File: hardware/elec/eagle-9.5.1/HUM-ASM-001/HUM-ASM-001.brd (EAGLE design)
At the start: 99.1 x 99.1 mm, 61 parts, among them J1 B2B-XH-AM(LF)(SN), J2 75869-131LF, J22 75869-131LF, J23 75869-131LF, K1 7-1393239-7, K2 7-1393239-7, Q1 IRLB8721PBF, Q2 IRLB8721PBF, U1 MCP23017-E/SP

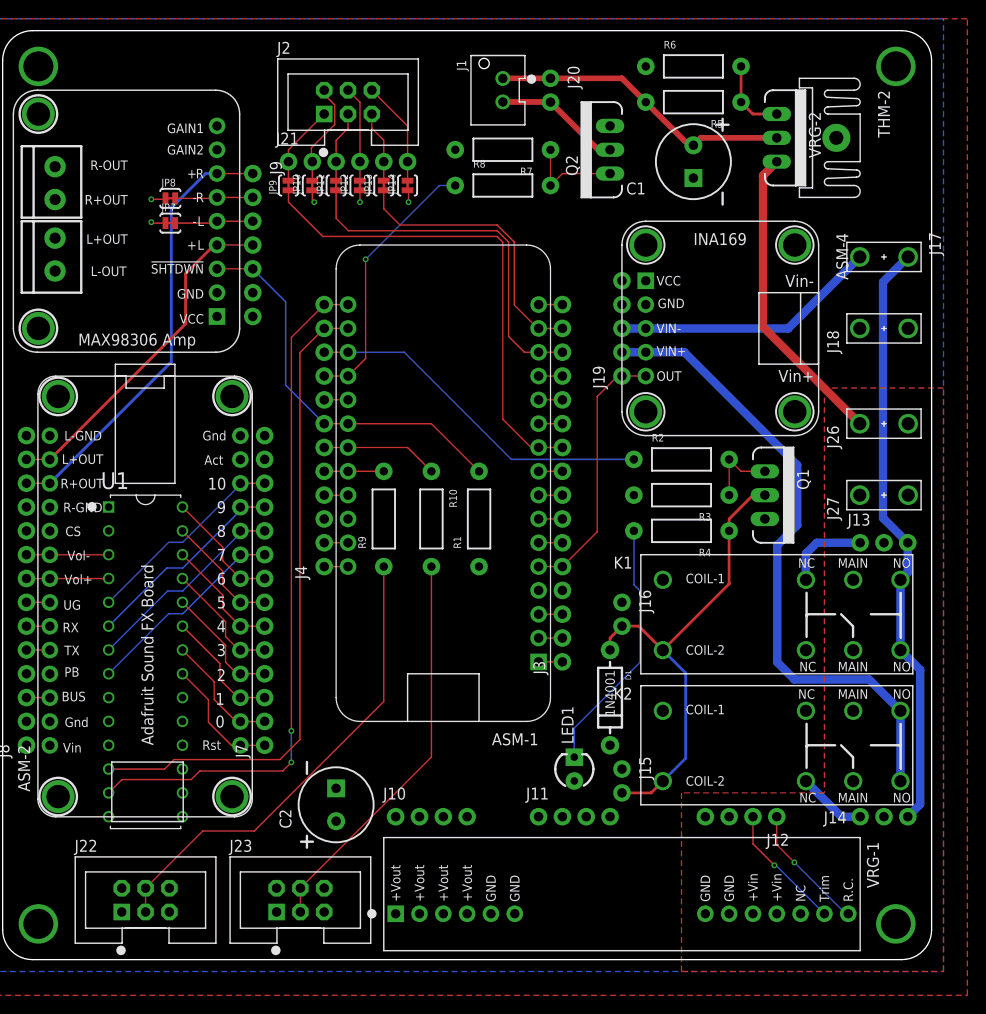
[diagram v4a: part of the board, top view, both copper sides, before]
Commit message: * Fixed crash / recovery inconsistency * Pre silk screen clean up
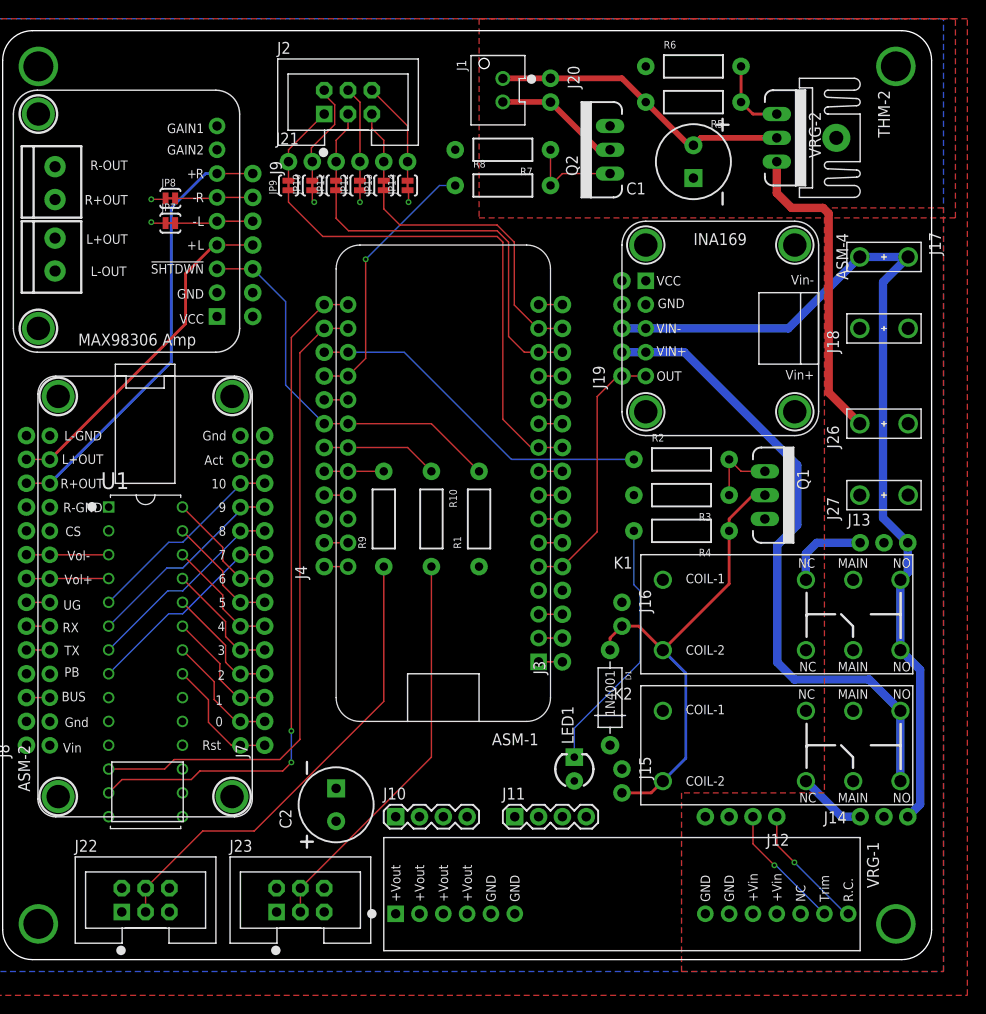
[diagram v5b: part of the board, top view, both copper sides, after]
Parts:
- J10, J11: device MG-Eagle_v1:1X04_NO_SILK_ALL_ROUND -> MG-Eagle_v1:1X04
- moved J11 2.54 mm to (54.6, 15.2)
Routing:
- net MIST-VIN: track 92.2 -> 97.3 mm
- net N$26: track 0.00 -> 2.59 mm
- net 48V: track 32.8 -> 33.6 mm
- added copper zone on layer 1, net 24V-CUTOUT
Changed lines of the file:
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@@
 <setting verticaltext="up"/>
 </settings>
-<grid distance="0.012" unitdist="inch" unit="inch" style="dots" multiple="1" display="yes" altdistance="0.006" altunitdist="inch" altunit="inch"/>
+<grid distance="0.05" unitdist="inch" unit="inch" style="dots" multiple="1" display="yes" altdistance="0.005" altunitdist="inch" altunit="inch"/>
 <layers>
 <layer number="1" name="Top" color="12" fill="1" visible="yes" active="yes"/>
@@
 <layer number="25" name="tNames" color="16" fill="1" visible="yes" active="yes"/>
 <layer number="26" name="bNames" color="7" fill="1" visible="yes" active="yes"/>
-<layer number="27" name="tValues" color="16" fill="1" visible="yes" active="yes"/>
-<layer number="28" name="bValues" color="7" fill="1" visible="yes" active="yes"/>
-<layer number="29" name="tStop" color="7" fill="3" visible="no" active="yes"/>
-<layer number="30" name="bStop" color="7" fill="6" visible="no" active="yes"/>
+<layer number="27" name="tValues" color="16" fill="1" visible="no" active="yes"/>
+<layer number="28" name="bValues" color="7" fill="1" visible="no" active="yes"/>
+<layer number="29" name="tStop" color="7" fill="3" visible="yes" active="yes"/>
+<layer number="30" name="bStop" color="7" fill="6" visible="yes" active="yes"/>
 <layer number="31" name="tCream" color="7" fill="4" visible="no" active="yes"/>
 <layer number="32" name="bCream" color="7" fill="5" visible="no" active="yes"/>
@@
 <layer number="45" name="Holes" color="7" fill="1" visible="yes" active="yes"/>
 <layer number="46" name="Milling" color="20" fill="1" visible="yes" active="yes"/>
-<layer number="47" name="Measures" color="5" fill="1" visible="no" active="yes"/>
+<layer number="47" name="Measures" color="5" fill="1" visible="yes" active="yes"/>
 <layer number="48" name="Document" color="6" fill="1" visible="yes" active="yes"/>
 <layer number="49" name="Reference" color="5" fill="1" visible="yes" active="yes"/>
@@
 <attribute name="VALUE" x="48.036" y="95.926" size="0.762" layer="27" ratio="11" rot="R270" align="top-left"/>
 </element>
-<element name="J10" library="MG-Eagle_v1" package="1X04_NO_SILK_ALL_ROUND" value="" x="41.91" y="15.24" smashed="yes">
+<element name="J10" library="MG-Eagle_v1" package="1X04" value="" x="41.91" y="15.24" smashed="yes">
 <attribute name="NAME" x="40.5638" y="17.0688" size="1.27" layer="25" ratio="10"/>
 <attribute name="PROD_ID" value="CONN-09696" x="146.05" y="-137.16" size="1.778" layer="27" display="off"/>
 <attribute name="VALUE" x="40.64" y="12.065" size="1.27" layer="27"/>
 </element>
-<element name="J11" library="MG-Eagle_v1" package="1X04_NO_SILK_ALL_ROUND" value="" x="57.15" y="15.24" smashed="yes">
-<attribute name="NAME" x="55.8038" y="17.0688" size="1.27" layer="25" ratio="10"/>
-<attribute name="PROD_ID" value="CONN-09696" x="172.72" y="-137.16" size="1.778" layer="27" display="off"/>
-<attribute name="VALUE" x="55.88" y="12.065" size="1.27" layer="27"/>
+<element name="J11" library="MG-Eagle_v1" package="1X04" value="" x="54.61" y="15.24" smashed="yes">
+<attribute name="NAME" x="53.2638" y="17.0688" size="1.27" layer="25" ratio="10"/>
+<attribute name="PROD_ID" value="CONN-09696" x="170.18" y="-137.16" size="1.778" layer="27" display="off"/>
+<attribute name="VALUE" x="53.34" y="12.065" size="1.27" layer="27"/>
 </element>
 <element name="J12" library="MG-Eagle_v1" package="1X04_NO_SILK_ALL_ROUND" value="" x="82.55" y="15.24" smashed="yes" rot="R180">
@@
 <wire x1="17.3736" y1="78.5368" x2="15.9512" y2="78.5368" width="0.1524" layer="1"/>
 <wire x1="15.9512" y1="78.5368" x2="15.8496" y2="78.6384" width="0.1524" layer="1"/>
+<wire x1="91.4019" y1="49.53" x2="96.5581" y2="49.53" width="0" layer="19" extent="1-1"/>
 </signal>
 <signal name="5V">
@@
 <contactref element="J26" pad="2"/>
 <polygon width="0.3048" layer="1" isolate="0.8128">
-<vertex x="100.33" y="60.96"/>
-<vertex x="87.63" y="60.96"/>
+<vertex x="100.33" y="80.1624"/>
+<vertex x="87.63" y="80.1624"/>
 <vertex x="87.63" y="17.78"/>
 <vertex x="72.39" y="17.78"/>
@@
 <vertex x="100.33" y="-1.27"/>
 </polygon>
-<wire x1="91.4019" y1="57.15" x2="81.0768" y2="67.4751" width="0.889" layer="1"/>
-<wire x1="81.0768" y1="83.6168" x2="82.55" y2="85.09" width="0.889" layer="1"/>
-<wire x1="81.0768" y1="67.4751" x2="81.0768" y2="83.6168" width="0.889" layer="1"/>
+<wire x1="91.4019" y1="57.15" x2="88.0872" y2="60.4647" width="0.889" layer="1"/>
+<wire x1="87.4776" y1="80.1624" x2="84.1248" y2="80.1624" width="0.889" layer="1"/>
+<wire x1="84.1248" y1="80.1624" x2="82.55" y2="81.7372" width="0.889" layer="1"/>
+<wire x1="82.55" y1="81.7372" x2="82.55" y2="85.09" width="0.889" layer="1"/>
+<wire x1="88.0872" y1="60.4647" x2="88.0872" y2="79.5528" width="0.889" layer="1"/>
+<wire x1="88.0872" y1="79.5528" x2="87.4776" y2="80.1624" width="0.889" layer="1"/>
 </signal>
 <signal name="N$27">
@@
 <wire x1="97.8408" y1="30.8992" x2="95.74" y2="33" width="0.889" layer="16"/>
 <wire x1="97.8408" y1="16.5608" x2="97.8408" y2="30.8992" width="0.889" layer="16"/>
-<wire x1="96.5581" y1="74.93" x2="91.4019" y2="74.93" width="0" layer="19" extent="1-1"/>
+<wire x1="91.4019" y1="74.93" x2="96.5581" y2="74.93" width="0.889" layer="16"/>
 </signal>
 <signal name="N$16">
@@
 <contactref element="ASM-2" pad="13"/>
 <contactref element="J7" pad="13"/>
-<wire x1="25.351" y1="53.327" x2="27.94" y2="53.34" width="0" layer="19" extent="1-1"/>
+<wire x1="25.351" y1="53.327" x2="25.364" y2="53.34" width="0.1524" layer="1"/>
+<wire x1="25.364" y1="53.34" x2="27.94" y2="53.34" width="0.1524" layer="1"/>
 </signal>
 <signal name="USB/VBUS">
@@
 <wire x1="22.7584" y1="81.1784" x2="22.86" y2="81.28" width="0.1524" layer="1"/>
 </signal>
+<signal name="24V-CUTOUT">
+<polygon width="0.3048" layer="1" pour="cutout" isolate="0.3048" rank="2">
+<vertex x="50.8" y="100.33"/>
+<vertex x="50.8" y="79.0956"/>
+<vertex x="101.6" y="79.0956"/>
+<vertex x="101.6" y="100.33"/>
+</polygon>
+</signal>
 </signals>

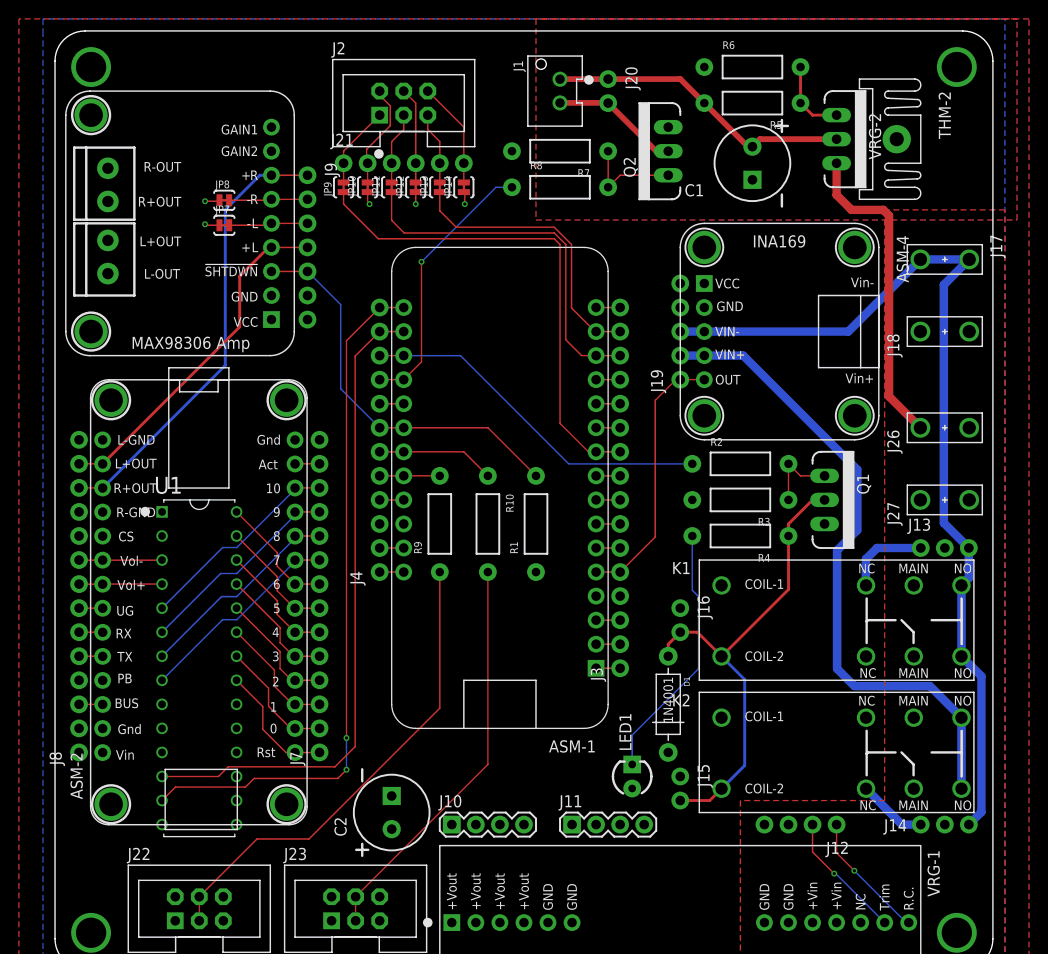
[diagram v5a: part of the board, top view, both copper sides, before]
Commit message: * Normalized Text for Names and Values
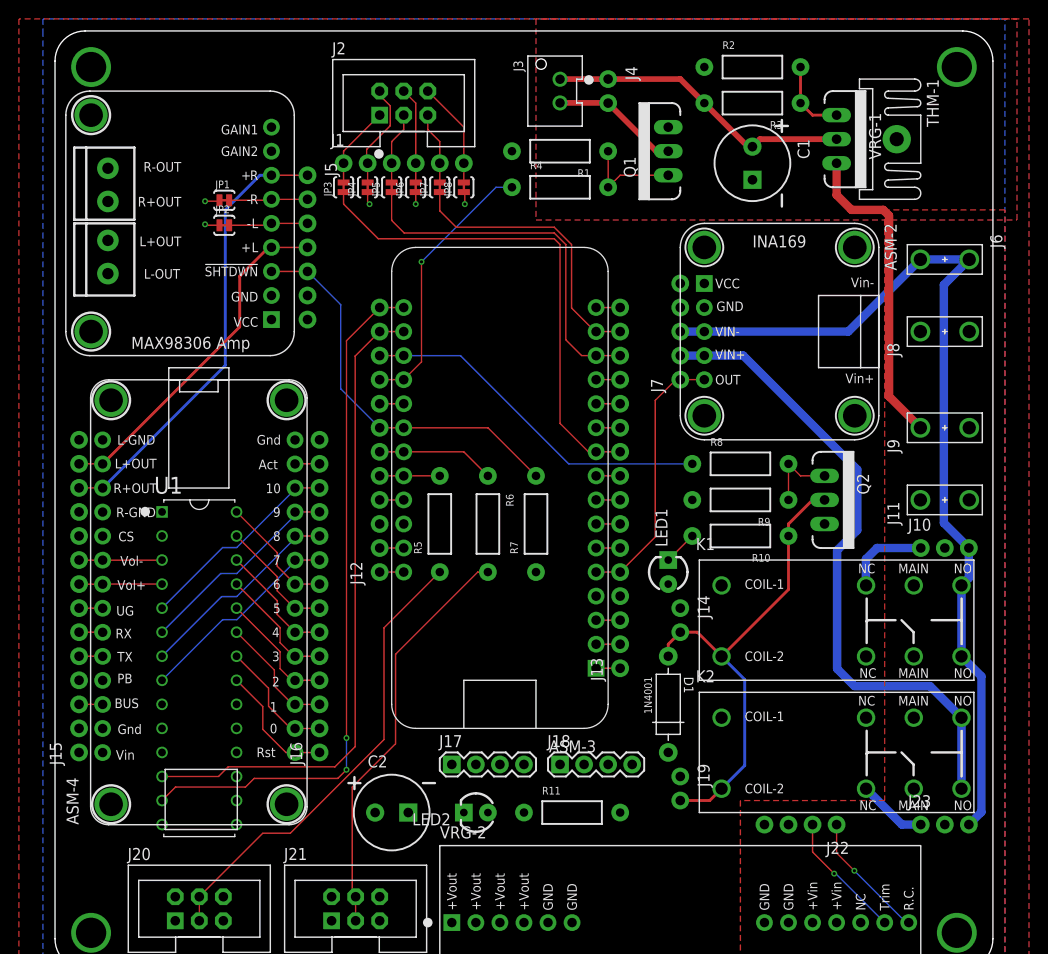
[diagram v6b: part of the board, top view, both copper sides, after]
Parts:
- removed J26, J27: (no value), MG-Eagle_v1:TE_1217861-1
- removed JP13, JP14: CON_JUMPER_PAD-2-NC_BY_TRACE, MG-Eagle_v1:PAD-JUMPER-2-NC_BY_TRACE_YES_SILK
- added J5: (no value), MG-Eagle_v1:1X07_NO_SILK
- added J6: (no value), MG-Eagle_v1:TE_1217861-1
- added JP1, JP2: CON_JUMPER_PAD-2-NC_BY_TRACE, MG-Eagle_v1:PAD-JUMPER-2-NC_BY_TRACE_YES_SILK
- added LED2: 3mm Green, MG-Eagle_v1:LED3MM
- added R11: 100, MG-Eagle_v1:AXIAL-0.4
- ASM-1: value Feather Bluefruit 32u4 -> (none); device MG-Eagle_v1:ASM_ADAFRUIT_FEATHER_BLUEFRUIT -> MG-Eagle_v1:ASM_ADAFRUIT_MAX98306_AMP_MOUNTING_HOLES
- ASM-2: device MG-Eagle_v1:ASM_ADAFRUIT_SOUND_FX_BOARD -> MG-Eagle_v1:ASM_ADAFRUIT_INA169_MOUNTING_HOLES
- ASM-3: value (none) -> Feather Bluefruit 32u4; device MG-Eagle_v1:ASM_ADAFRUIT_MAX98306_AMP_MOUNTING_HOLES -> MG-Eagle_v1:ASM_ADAFRUIT_FEATHER_BLUEFRUIT
- ASM-4: device MG-Eagle_v1:ASM_ADAFRUIT_INA169_MOUNTING_HOLES -> MG-Eagle_v1:ASM_ADAFRUIT_SOUND_FX_BOARD
- J1: value B2B-XH-AM(LF)(SN) -> (none); device MG-Eagle_v1:JST-2-PTH-VERT_XH -> MG-Eagle_v1:1X06_NO_SILK
- J10: device MG-Eagle_v1:1X04 -> MG-Eagle_v1:1X03_NO_SILK
- J11: device MG-Eagle_v1:1X04 -> MG-Eagle_v1:TE_1217861-1
- J12: device MG-Eagle_v1:1X04_NO_SILK_ALL_ROUND -> MG-Eagle_v1:1X12_NO_SILK
- J13: device MG-Eagle_v1:1X03_NO_SILK -> MG-Eagle_v1:1X16_NO_SILK
- J14: device MG-Eagle_v1:1X03_NO_SILK -> MG-Eagle_v1:1X02_NO_SILK
- J15, J16: device MG-Eagle_v1:1X02_NO_SILK -> MG-Eagle_v1:1X14_NO_SILK
- J17, J18: device MG-Eagle_v1:TE_1217861-1 -> MG-Eagle_v1:1X04
- J19: device MG-Eagle_v1:1X05_NO_SILK -> MG-Eagle_v1:1X02_NO_SILK
- J20: value (none) -> 75869-131LF; device MG-Eagle_v1:1X02_NO_SILK -> MG-Eagle_v1:2X3-SHROUDED
- J21: value (none) -> 75869-131LF; device MG-Eagle_v1:1X06_NO_SILK -> MG-Eagle_v1:2X3-SHROUDED
- J22: value 75869-131LF -> (none); device MG-Eagle_v1:2X3-SHROUDED -> MG-Eagle_v1:1X04_NO_SILK_ALL_ROUND
- J23: value 75869-131LF -> (none); device MG-Eagle_v1:2X3-SHROUDED -> MG-Eagle_v1:1X03_NO_SILK
- J3: value (none) -> B2B-XH-AM(LF)(SN); device MG-Eagle_v1:1X16_NO_SILK -> MG-Eagle_v1:JST-2-PTH-VERT_XH
- J4: device MG-Eagle_v1:1X12_NO_SILK -> MG-Eagle_v1:1X02_NO_SILK
- J7: device MG-Eagle_v1:1X14_NO_SILK -> MG-Eagle_v1:1X05_NO_SILK
- J8: device MG-Eagle_v1:1X14_NO_SILK -> MG-Eagle_v1:TE_1217861-1
- J9: device MG-Eagle_v1:1X07_NO_SILK -> MG-Eagle_v1:TE_1217861-1
- R1: value 1k -> 10k
- R2: value 100 -> 4k, 1%
- R3: value 10k -> 220
- R5: value 220 -> 100
- R6: value 4k, 1% -> 100
- R7: value 10k -> 1k
- R9: value 100 -> 10k
- VRG-1: value NID100-5 -> LM317; device MG-Eagle_v1:VRG_NID100-X -> MG-Eagle_v1:TO-220-VERTICAL
- VRG-2: value LM317 -> NID100-5; device MG-Eagle_v1:TO-220-VERTICAL -> MG-Eagle_v1:VRG_NID100-X
- moved MH3 129.3 mm to (3.81, 3.81)
- moved J8 101.7 mm to (94.0, 67.3), turned to 0 degrees
- moved J20 97.7 mm to (15.2, 6.35), turned to 0 degrees
- moved MH1 91.4 mm to (3.81, 95.2)
- moved MH2 91.4 mm to (95.2, 95.2)
- moved VRG-1 82.4 mm to (82.5, 87.6), turned to 270 degrees
- moved VRG-2 82.4 mm to (66.0, 6.89), turned to 0 degrees
- moved J21 78.8 mm to (31.8, 6.35)
- moved J17 74.5 mm to (41.9, 21.6), turned to 0 degrees
- moved J9 72.4 mm to (94.0, 57.1), turned to 0 degrees
- moved ASM-2 68.3 mm to (77.5, 67.3), turned to 270 degrees
- moved ASM-4 68.3 mm to (15.6, 38.2), turned to 90 degrees
- moved J22 67.9 mm to (82.5, 15.2), turned to 180 degrees
- moved J15 63.6 mm to (2.54, 22.9), turned to 90 degrees
- moved J3 61.3 mm to (53.3, 92.7), turned to 270 degrees
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- renumbered JP10 to JP4, JP11 to JP5, JP12 to JP6, JP9 to JP3, THM-2 to THM-1
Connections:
- new net N$19: LED2.A, R11.P$1
- net !AMP-SHDN: now also ASM-1.3, ASM-3.D10, J12.7, J5.5, R7.P$2; no longer ASM-1.D10, ASM-3.3, J4.7, J9.5, R1.P$2
- net 24V: now also J3.1, J4.1, R3.P$2, VRG-1.P2; no longer J1.1, J20.1, R5.P$2, VRG-2.P2
- net 3V: now also ASM-3.3V3, J13.2; no longer ASM-1.3V3, J3.2
- net 48V: now also J10.2, J22.3, J22.4, J23.2, J9.1, J9.2, VRG-1.P3, VRG-2.P$10, VRG-2.P$9; no longer J12.3, J12.4, J13.2, J14.2, J26.1, J26.2, VRG-1.P$10, VRG-1.P$9, VRG-2.P3
- net 5V: now also ASM-1.1, ASM-2.1, ASM-3.USB/VBUS, ASM-4.28, J12.3, J14.1, J17.1, J17.2, J17.3, J17.4, J19.1, J20.1, J20.2, J21.1, J21.2, J5.7, J7.5, LED2.K, VRG-2.P$1, VRG-2.P$2, VRG-2.P$3, VRG-2.P$4; no longer ASM-1.USB/VBUS, ASM-2.28, ASM-3.1, ASM-4.1, J10.1, J10.2, J10.3, J10.4, J16.1, J19.5, J22.1, J22.2, J23.1, J23.2, J4.3, J8.1, J9.7, VRG-1.P$1, VRG-1.P$2, VRG-1.P$3, VRG-1.P$4
- net ADJ: now also R2.P$2, R3.P$1, VRG-1.P1; no longer R5.P$1, R6.P$2, VRG-2.P1
- net CRNT-MON: now also ASM-2.5, ASM-3.A0, J13.5, J7.1; no longer ASM-1.A0, ASM-4.5, J19.1, J3.5
- net DFU: now also ASM-3.DFU, J13.16; no longer ASM-1.DFU, J3.16
- net ENCODER-A: now also ASM-3.RX0, J13.14; no longer ASM-1.RX0, J3.14
- net ENCODER-B: now also ASM-3.TX1, J13.15, JP7.1; no longer ASM-1.TX1, J3.15, JP13.1
- net ENCODER-SW: now also ASM-3.A5, J13.10; no longer ASM-1.A5, J3.10
- net FAN-CTRL: now also ASM-3.D6, J12.9, R4.P$1; no longer ASM-1.D6, J4.9, R8.P$1
- net GND: now also ASM-1.2, ASM-2.2, ASM-3.GND@4, ASM-4.14, ASM-4.15, ASM-4.18, ASM-4.27, J13.4, J15.11, J15.14, J15.2, J16.14, J18.3, J18.4, J20.5, J20.6, J21.5, J21.6, J5.6, J7.4, J8.1, JP1.1, JP2.1, R1.P$2, R11.P$2, R2.P$1, R7.P$1, R9.P$2, VRG-2.P$5, VRG-2.P$6, VRG-2.P$7, VRG-2.P$8; no longer ASM-1.GND@4, ASM-2.14, ASM-2.15, ASM-2.18, ASM-2.27, ASM-3.2, ASM-4.2, J11.3, J11.4, J19.4, J22.5, J22.6, J23.5, J23.6, J27.1, J27.2, J3.4, J7.14, J8.11, J8.14, J9.6, JP14.1, JP7.1, R1.P$1, R3.P$2, R6.P$1, R7.P$2, VRG-1.P$5, VRG-1.P$6, VRG-1.P$7, VRG-1.P$8
- net I2C-SCL: now also ASM-3.SCL, J12.11; no longer ASM-1.SCL, J4.11
- net I2C-SDA: now also ASM-3.SDA, J12.12; no longer ASM-1.SDA, J4.12
- net K1-NC: now also J10.1; no longer J13.1
- net K2-NC: now also J23.1; no longer J14.1
- net LED1-DATA: now also ASM-3.D12, J12.5, R5.P$2; no longer ASM-1.D12, J4.5, R9.P$2
- net LED2-DATA: now also ASM-3.D11, J12.6, R6.P$1; no longer ASM-1.D11, J4.6, R10.P$1
- net MIST-CTRL: now also ASM-3.D5, J12.10, R8.P$1; no longer ASM-1.D5, J4.10, R2.P$1
- net MIST-VIN: now also ASM-2.3, J10.3, J23.3, J6.1, J6.2, J7.3; no longer ASM-4.3, J13.3, J14.3, J17.1, J17.2, J19.3
- net N$1: now also ASM-3.!RESET, J13.1; no longer ASM-1.!RESET, J3.1
- net N$10: now also J14.2, J19.2, Q2.P2, R10.P$1; no longer J15.2, J16.2, Q1.P2, R4.P$1
- net N$11: now also Q2.P1, R8.P$2, R9.P$1; no longer Q1.P1, R2.P$2, R3.P$1
- net N$12: now also J3.2, J4.2, Q1.P2; no longer J1.2, J20.2, Q2.P2
- net N$13: now also R10.P$2; no longer R4.P$2
- net N$14: now also ASM-1.5, J5.3, JP2.2; no longer ASM-3.5, J9.3, JP7.2
- net N$15: now also ASM-1.6, J5.2, JP1.2; no longer ASM-3.6, J9.2, JP8.2
- net N$16: now also ASM-2.4, J7.2; no longer ASM-4.4, J19.2
- net N$17: now also Q1.P1, R1.P$1, R4.P$2; no longer Q2.P1, R7.P$1, R8.P$2
- net N$18: now also J1.1; no longer J21.1
- net N$2: now also ASM-3.AREF, J13.3; no longer ASM-1.AREF, J3.3
- net N$20: now also ASM-3.D9, J12.8; no longer ASM-1.D9, J4.8
- net N$21: now also J1.2; no longer J21.2
- net N$22: now also J1.3; no longer J21.3
- net N$24: now also ASM-3.D13, J12.4; no longer ASM-1.D13, J4.4
- net N$25: now also ASM-3.EN, J12.2; no longer ASM-1.EN, J4.2
- net N$26: now also ASM-4.13, J16.13; no longer ASM-2.13, J7.13
- net N$27: now also J22.1, VRG-2.P$13; no longer J12.1, VRG-1.P$13
- net N$29: now also J22.2, VRG-2.P$12; no longer J12.2, VRG-1.P$12
- net N$30: now also ASM-4.24, J15.5; no longer ASM-2.24, J8.5
- net N$31: now also ASM-4.23, J15.6; no longer ASM-2.23, J8.6
- net N$38: now also ASM-4.22, J15.7; no longer ASM-2.22, J8.7
- net N$39: now also J1.4; no longer J21.4
- net N$40: now also J1.5, JP7.2; no longer J21.5, JP13.2
- net N$41: now also J1.6, JP8.2; no longer J21.6, JP14.2
- net N$42: now also J21.3, J21.4, R6.P$2; no longer J23.3, J23.4, R10.P$2
- net N$5: now also ASM-3.A1, J13.6; no longer ASM-1.A1, J3.6
- net N$6: now also ASM-3.A2, J13.7; no longer ASM-1.A2, J3.7
- net N$7: now also ASM-3.A3, J13.8; no longer ASM-1.A3, J3.8
- net N$8: now also ASM-3.A4, J13.9; no longer ASM-1.A4, J3.9
- net N$9: now also J20.3, J20.4, R5.P$1; no longer J22.3, J22.4, R9.P$1
- net SFX-0: now also ASM-4.2, J16.2; no longer ASM-2.2, J7.2
- net SFX-1: now also ASM-4.3, J16.3; no longer ASM-2.3, J7.3
- net SFX-10: now also ASM-4.12, J16.12; no longer ASM-2.12, J7.12
- net SFX-2: now also ASM-4.4, J16.4; no longer ASM-2.4, J7.4
- net SFX-3: now also ASM-4.5, J16.5; no longer ASM-2.5, J7.5
- net SFX-4: now also ASM-4.6, J16.6; no longer ASM-2.6, J7.6
- net SFX-5: now also ASM-4.7, J16.7; no longer ASM-2.7, J7.7
- net SFX-6: now also ASM-4.8, J16.8; no longer ASM-2.8, J7.8
- net SFX-7: now also ASM-4.9, J16.9; no longer ASM-2.9, J7.9
- net SFX-8: now also ASM-4.10, J16.10; no longer ASM-2.10, J7.10
- net SFX-9: now also ASM-4.11, J16.11; no longer ASM-2.11, J7.11
- net SFX-LOUT: now also ASM-1.4, ASM-4.16, J15.13, J5.4; no longer ASM-2.16, ASM-3.4, J8.13, J9.4
- net SFX-ROUT: now also ASM-1.7, ASM-4.17, J15.12, J5.1; no longer ASM-2.17, ASM-3.7, J8.12, J9.1
- net SFX-RST: now also ASM-4.1, J16.1; no longer ASM-2.1, J7.1
- net SFX-VOL-N: now also ASM-4.20, J15.9; no longer ASM-2.20, J8.9
- net SFX-VOL-P: now also ASM-4.21, J15.8; no longer ASM-2.21, J8.8
- net SPI-MISO: now also ASM-3.MISO, J13.13; no longer ASM-1.MISO, J3.13
- net SPI-MOSI: now also ASM-3.MOSI, J13.12; no longer ASM-1.MOSI, J3.12
- net SPI-SCK: now also ASM-3.SCK, J13.11; no longer ASM-1.SCK, J3.11
- net USB/VBUS: now also ASM-4.26, J15.3; no longer ASM-2.26, J8.3
- net VBAT: now also ASM-3.VBAT, J12.1; no longer ASM-1.VBAT, J4.1
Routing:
- net N$13: track 27.3 -> 3.59 mm
- net N$9: track 50.6 -> 49.1 mm
- net N$42: track 42.6 -> 43.5 mm
